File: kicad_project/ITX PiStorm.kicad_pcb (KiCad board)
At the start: 4 copper layers, 170 x 170 mm, 18 parts, among them J2 USB_67298-4090, J201 ATX-20, J3 DB9_Male_MountingHoles, J301 Conn_02x17_Odd_Even, J4 DB9_Male_MountingHoles, J5 HDMI_A_1.4, J6 DB15_Female_HighDensity, U301 74LVC06, U302 74LVC06, U303 74LVC14

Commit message: playground start
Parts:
- added U101: W25Q128JVS, Package_SO:SOIC-8_5.23x5.23mm_P1.27mm, F.Cu at (93.5, 158.8)
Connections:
- J201 pad 1: /Floppy Interface/+3.3V -> +3V3
- J201 pad 11: /Floppy Interface/+3.3V -> +3V3
- J201 pad 2: /Floppy Interface/+3.3V -> +3V3
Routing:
- net /Floppy Interface/+3.3V: track 42.5 -> 47.8 mm
- net /Floppy Interface/~{MTRON}: track 22.7 -> 21.9 mm

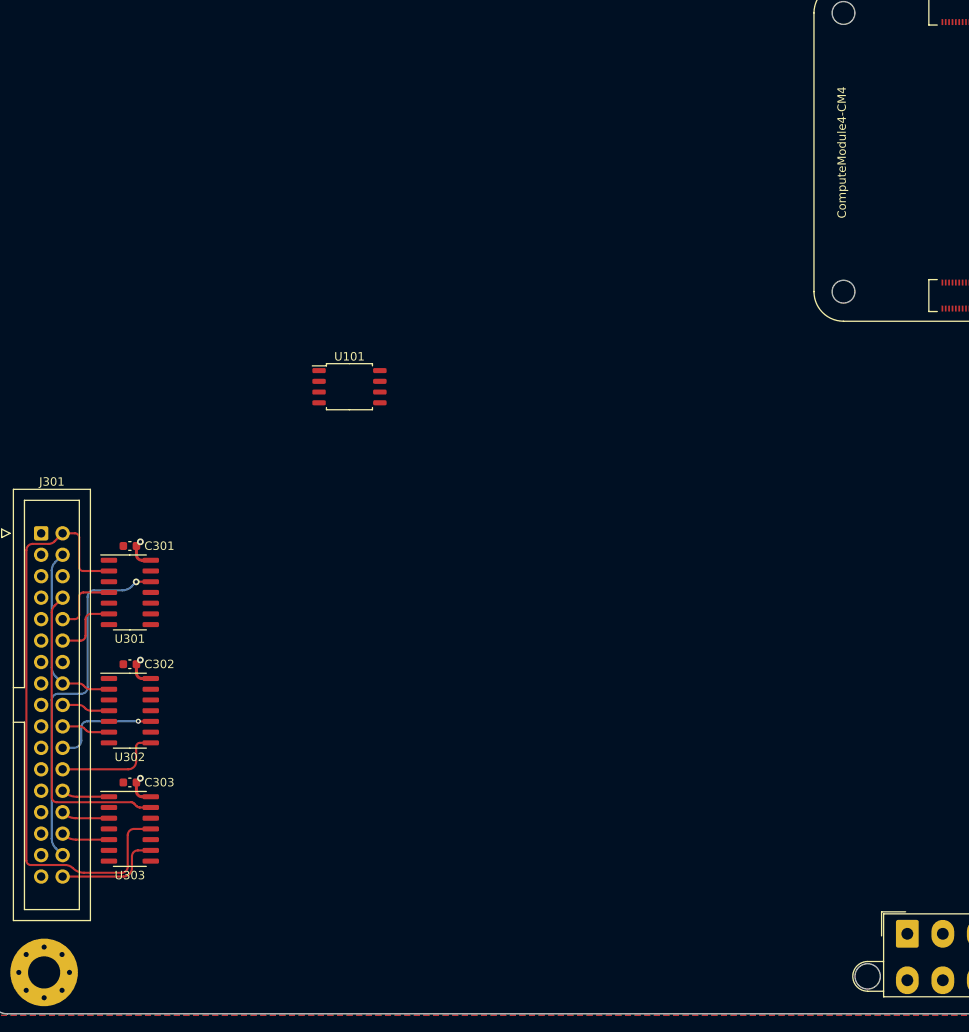
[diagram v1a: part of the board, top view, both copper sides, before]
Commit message: added ecp5 fpga without anything connected yet, added power to fpga
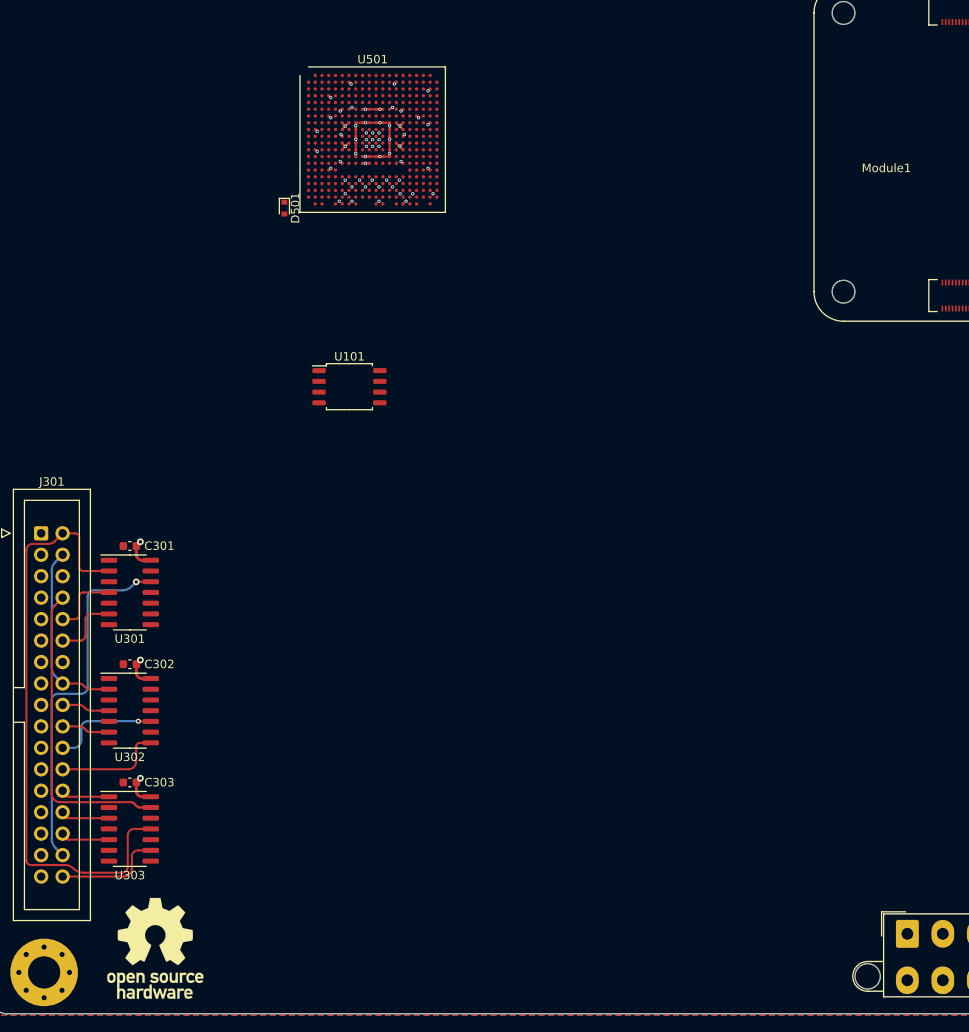
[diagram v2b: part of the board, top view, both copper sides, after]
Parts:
- added D501: 1N4148WT, Diode_SMD:D_SOD-523, F.Cu at (85.8, 137.6)
- added REF**: OSHW-Logo_11.4x12mm_SilkScreen, Symbol:OSHW-Logo_11.4x12mm_SilkScreen, F.Cu at (70.5, 225.2)
- added U501: LFE5U-85F-6BG381x, Package_BGA:Lattice_caBGA-381_17.0x17.0mm_Layout20x20_P0.8mm_Ball0.4mm_Pad0.4mm_NSMD, F.Cu at (96.2, 129.5)
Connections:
- C301 pad 1: /Floppy Interface/+3.3V -> +3V3
- C302 pad 1: /Floppy Interface/+3.3V -> +3V3
- C303 pad 1: /Floppy Interface/+3.3V -> +3V3
- U301 pad 14: /Floppy Interface/+3.3V -> +3V3
- U302 pad 14: /Floppy Interface/+3.3V -> +3V3
- U303 pad 14: /Floppy Interface/+3.3V -> +3V3
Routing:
- net +3V3: track 0.00 -> 57.9 mm, vias 0 -> 10
- net /Floppy Interface/+3.3V: track 47.8 -> 0.00 mm, vias 3 -> 0
- net +2V5: track 0.00 -> 26.9 mm, vias 0 -> 4
- net +1V2: track 0.00 -> 15.2 mm, vias 0 -> 10
- net GND: track 0.00 -> 3.54 mm, vias 0 -> 41
- added copper zone on In2.Cu, net +1V2
- added copper zone on In2.Cu, net +3V3
- removed copper zone on In2.Cu, net /Floppy Interface/+3.3V

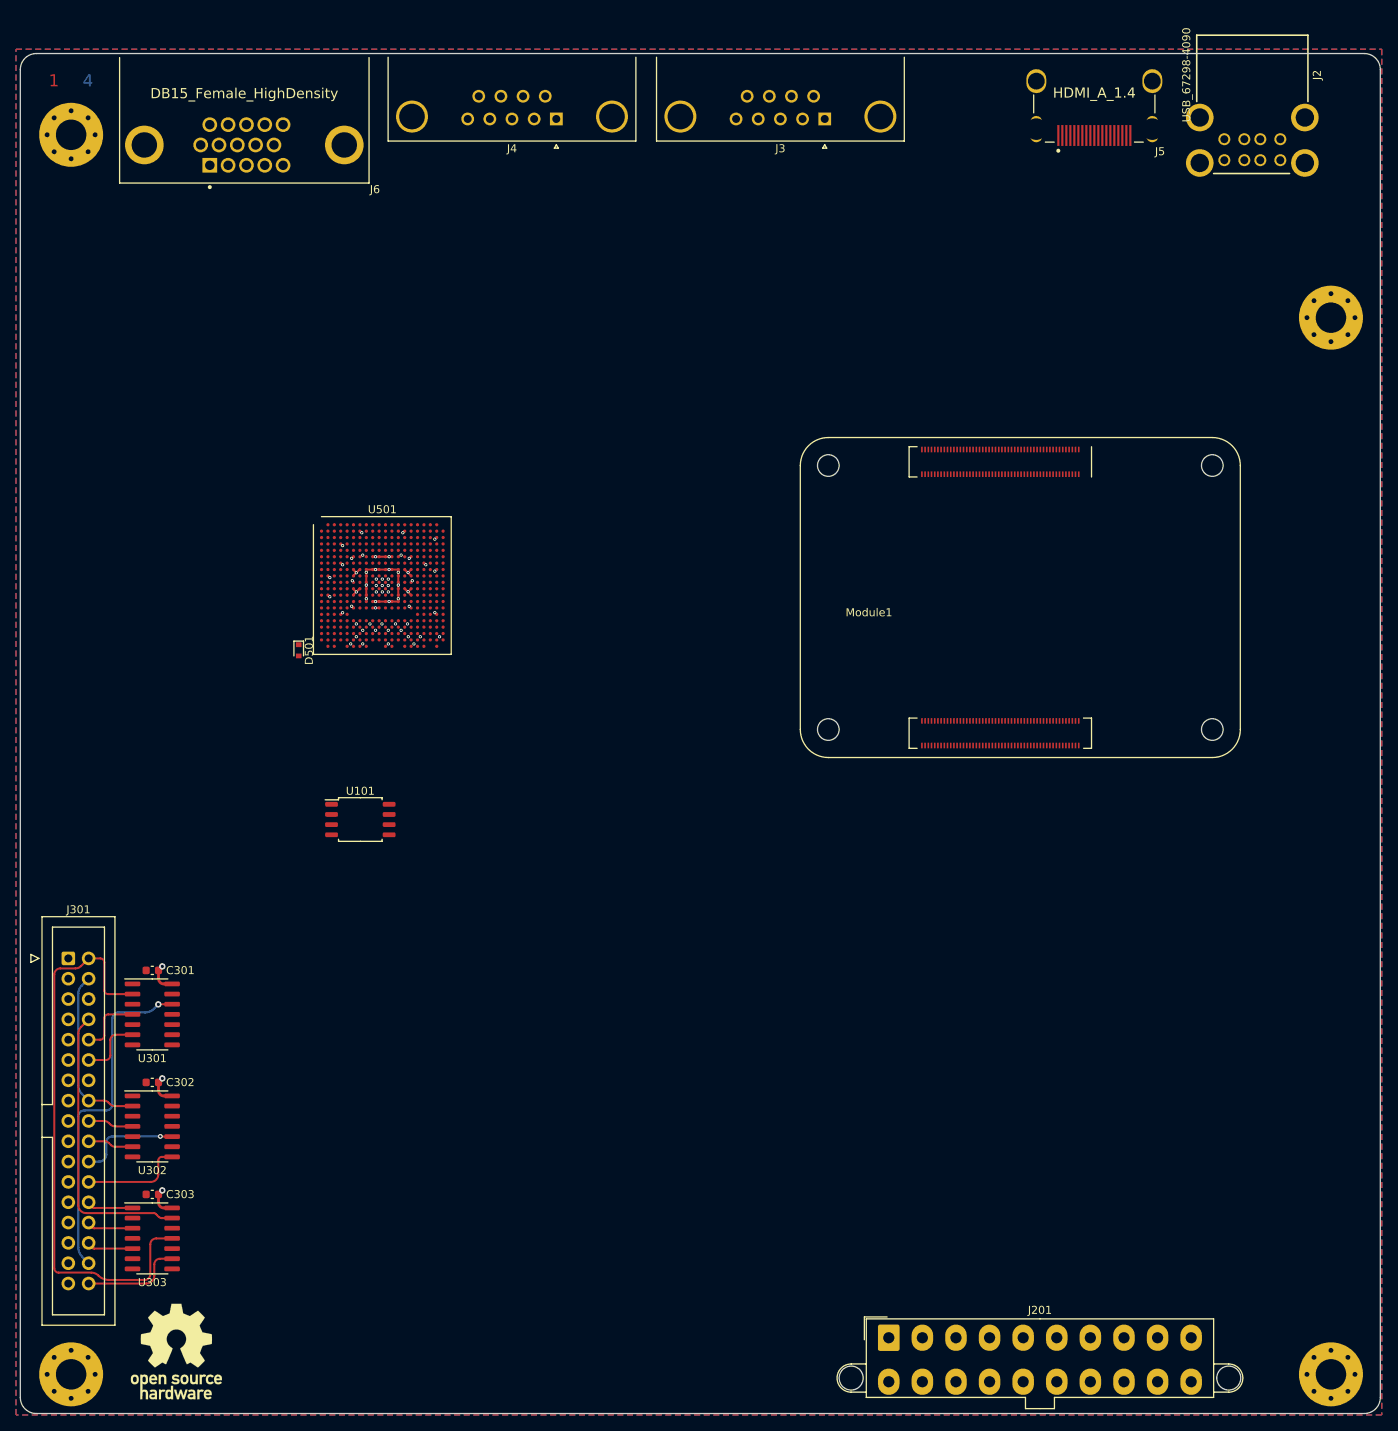
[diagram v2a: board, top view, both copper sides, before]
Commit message: added bits and pieces: a bit of memory, a bit of 1.1V power
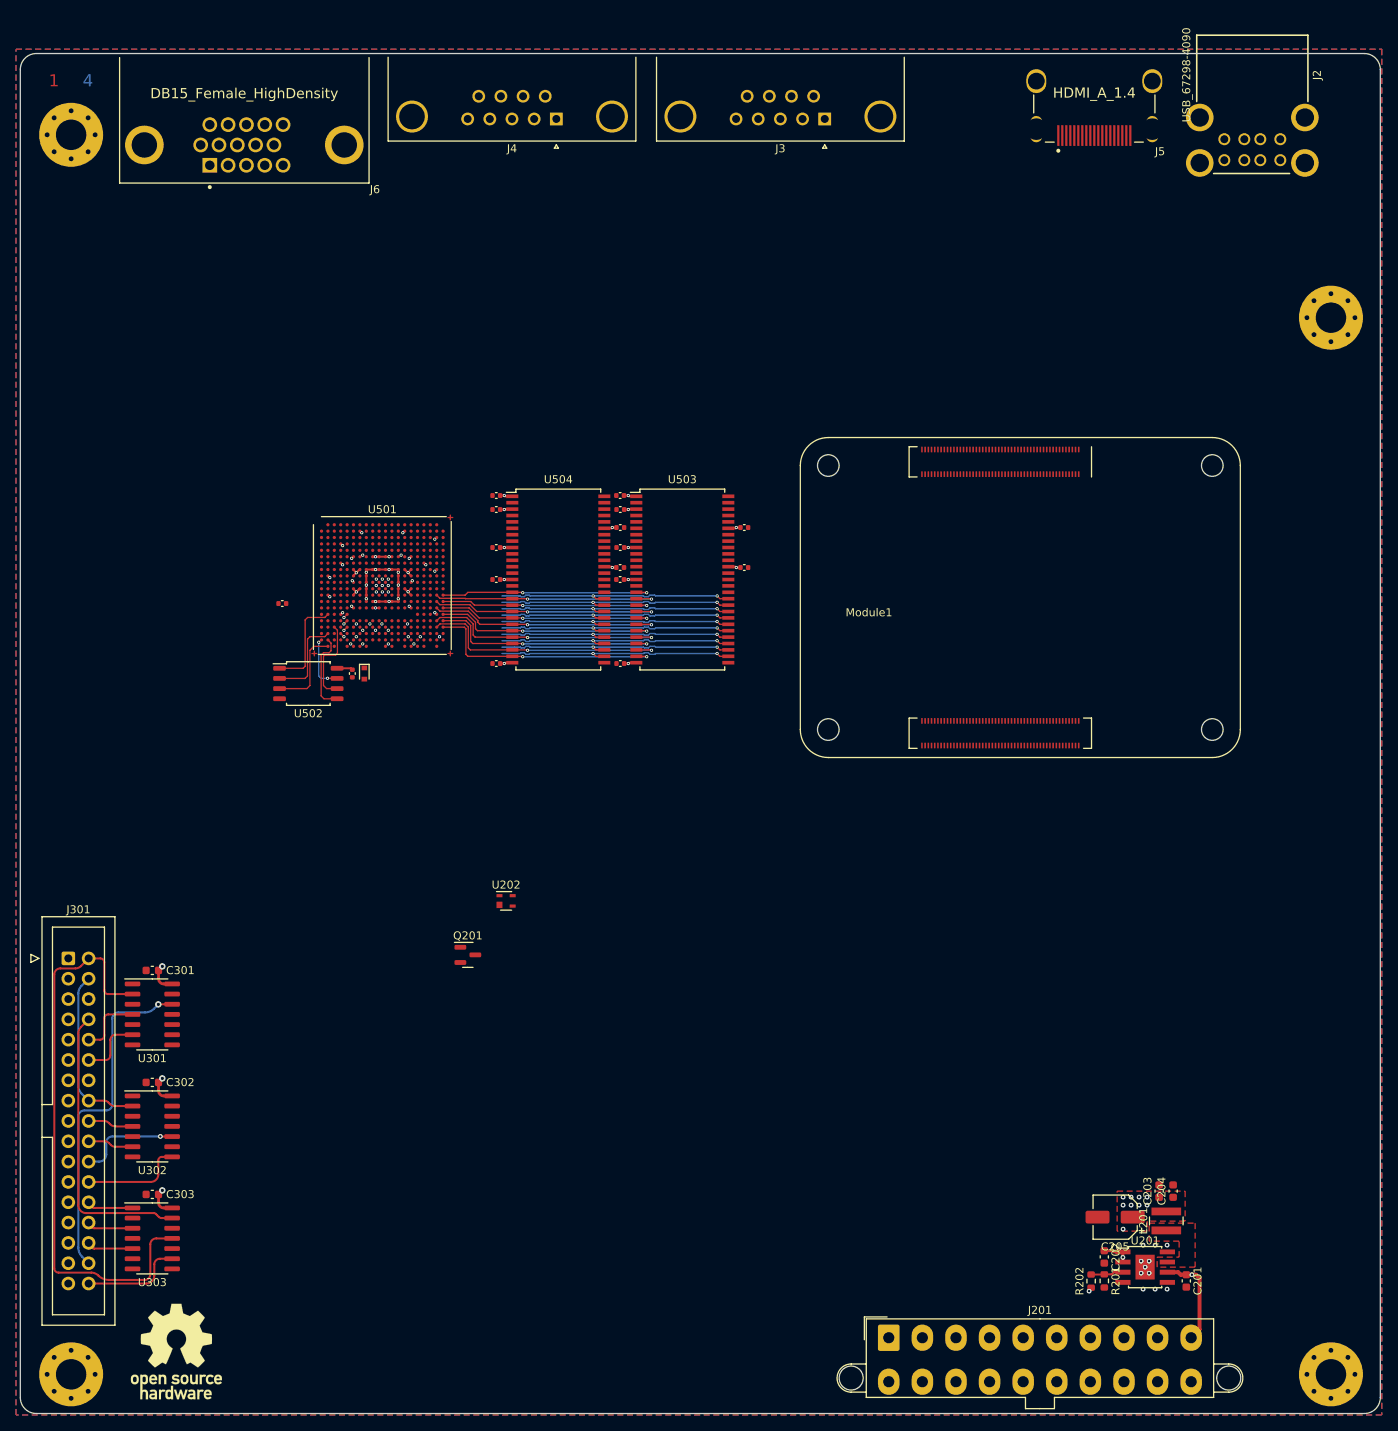
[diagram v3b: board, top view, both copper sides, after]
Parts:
- removed U101: W25Q128JVS, Package_SO:SOIC-8_5.23x5.23mm_P1.27mm
- added C201: 10µ, Capacitor_SMD:C_0603_1608Metric, F.Cu at (196.7, 216.4)
- added C202: 100nF, Capacitor_SMD:C_0603_1608Metric, F.Cu at (186.5, 213.4)
- added C203: 22µ, Capacitor_SMD:C_0603_1608Metric, F.Cu at (193.3, 205.2)
- added C204: 22µ, Capacitor_SMD:C_0603_1608Metric, F.Cu at (195.1, 205.2)
- added C205: 100µ, Capacitor_SMD:CP_Elec_5x5.9, F.Cu at (187.8, 208.4)
- added C501: 100nF, Capacitor_SMD:C_0402_1005Metric, F.Cu at (92.5, 140.5)
- added C502: 100nF, Capacitor_SMD:C_0402_1005Metric, F.Cu at (83.8, 131.8)
- added C503: 100nF, Capacitor_SMD:C_0402_1005Metric, F.Cu at (110.5, 128.8)
- added C504: 100nF, Capacitor_SMD:C_0402_1005Metric, F.Cu at (110.5, 124.8)
- added C505: 100nF, Capacitor_SMD:C_0402_1005Metric, F.Cu at (126.0, 127.2)
- added C506: 100nF, Capacitor_SMD:C_0402_1005Metric, F.Cu at (110.5, 120.0)
- added C507: 100nF, Capacitor_SMD:C_0402_1005Metric, F.Cu at (126.0, 122.2)
- added C508: 100nF, Capacitor_SMD:C_0402_1005Metric, F.Cu at (110.5, 118.2)
- added C509: 100nF, Capacitor_SMD:C_0402_1005Metric, F.Cu at (110.5, 139.2)
- added C510: 100nF, Capacitor_SMD:C_0402_1005Metric, F.Cu at (126.0, 124.8)
- added C511: 100nF, Capacitor_SMD:C_0402_1005Metric, F.Cu at (126.0, 120.0)
- added C512: 100nF, Capacitor_SMD:C_0402_1005Metric, F.Cu at (126.0, 128.8)
- added C513: 100nF, Capacitor_SMD:C_0402_1005Metric, F.Cu at (126.0, 118.2)
- added C514: 100nF, Capacitor_SMD:C_0402_1005Metric, F.Cu at (126.0, 139.2)
- added C515: 100nF, Capacitor_SMD:C_0402_1005Metric, F.Cu at (141.5, 127.2)
- added C516: 100nF, Capacitor_SMD:C_0402_1005Metric, F.Cu at (141.5, 122.2)
- added L201: 2.2µ, Inductor_SMD:L_Wuerth_MAPI-4030, F.Cu at (194.2, 208.9)
- added Q201: DMG2301L, Package_TO_SOT_SMD:SOT-23, F.Cu at (106.9, 175.7)
- added R201: 20k, Resistor_SMD:R_0603_1608Metric, F.Cu at (186.5, 216.4)
- added R202: 7k5, Resistor_SMD:R_0603_1608Metric, F.Cu at (184.8, 216.4)
- added U201: ST1S10PHR, Package_SO:TI_SO-PowerPAD-8, F.Cu at (191.6, 214.7)
- added U202: ADCMP350, Package_TO_SOT_SMD:Analog_KS-4, F.Cu at (111.7, 168.9)
- added U502: W25Q128JVS, Package_SO:SOIC-8_5.23x5.23mm_P1.27mm, F.Cu at (87.0, 141.8)
- added U503: MT48LC16M16A2P, Package_SO:TSOP-II-54_22.2x10.16mm_P0.8mm, F.Cu at (133.8, 128.8)
- added U504: MT48LC16M16A2P, Package_SO:TSOP-II-54_22.2x10.16mm_P0.8mm, F.Cu at (118.2, 128.8)
- moved D501 8.70 mm to (94.0, 140.5)
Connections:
- net +1V2 renamed +1V1
- U501 pad M19: unconnected-(U501-PadM19) -> /Memory and Bus Interface/~{CAS}
- U501 pad M20: unconnected-(U501-PadM20) -> /Memory and Bus Interface/~{WE}
- U501 pad N19: unconnected-(U501-PadN19) -> /Memory and Bus Interface/~{CS}
- U501 pad N20: unconnected-(U501-PadN20) -> /Memory and Bus Interface/~{RAS}
- U501 pad P19: unconnected-(U501-PadP19) -> /Memory and Bus Interface/BA1
- U501 pad P20: unconnected-(U501-PadP20) -> /Memory and Bus Interface/BA0
- U501 pad R2: unconnected-(U501-PadR2) -> Net-(U501-PadR2)
- U501 pad R20: unconnected-(U501-PadR20) -> /Memory and Bus Interface/A10
- U501 pad T19: unconnected-(U501-PadT19) -> /Memory and Bus Interface/A0
- U501 pad T20: unconnected-(U501-PadT20) -> /Memory and Bus Interface/A1
- U501 pad T4: unconnected-(U501-PadT4) -> +3V3
- U501 pad U19: unconnected-(U501-PadU19) -> /Memory and Bus Interface/A2
- U501 pad U20: unconnected-(U501-PadU20) -> /Memory and Bus Interface/A3
- U501 pad U3: unconnected-(U501-PadU3) -> Net-(U501-PadU3)
- U501 pad V2: unconnected-(U501-PadV2) -> Net-(U501-PadV2)
- U501 pad W1: unconnected-(U501-PadW1) -> Net-(U501-PadW1)
- U501 pad W2: unconnected-(U501-PadW2) -> Net-(U501-PadW2)
- U501 pad Y2: unconnected-(U501-PadY2) -> Net-(U501-PadY2)
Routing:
- net /Memory and Bus Interface/A2: track 0.00 -> 31.8 mm, vias 0 -> 2
- net /Memory and Bus Interface/A0: track 0.00 -> 30.8 mm, vias 0 -> 2
- net /Memory and Bus Interface/A11: track 0.00 -> 30.3 mm, vias 0 -> 2
- net /Memory and Bus Interface/A5: track 0.00 -> 30.3 mm, vias 0 -> 2
- net /Memory and Bus Interface/CLK: track 0.00 -> 30.3 mm, vias 0 -> 2
- net /Memory and Bus Interface/A8: track 0.00 -> 30.3 mm, vias 0 -> 2
- net /Memory and Bus Interface/A4: track 0.00 -> 30.3 mm, vias 0 -> 2
- net /Memory and Bus Interface/CKE: track 0.00 -> 30.3 mm, vias 0 -> 2
- net /Memory and Bus Interface/A9: track 0.00 -> 30.3 mm, vias 0 -> 2
- net /Memory and Bus Interface/A7: track 0.00 -> 30.3 mm, vias 0 -> 2
- net /Memory and Bus Interface/A6: track 0.00 -> 30.3 mm, vias 0 -> 2
- net /Memory and Bus Interface/A12: track 0.00 -> 30.3 mm, vias 0 -> 2
- net /Memory and Bus Interface/A3: track 0.00 -> 30.2 mm, vias 0 -> 2
- net /Memory and Bus Interface/BA1: track 0.00 -> 29.8 mm, vias 0 -> 2
- net /Memory and Bus Interface/~{CS}: track 0.00 -> 29.3 mm, vias 0 -> 2
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- added copper zone on F.Cu, net +1V1
- added copper zone on F.Cu, net Net-(L201-Pad1)

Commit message: minor wip updates
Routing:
- net /Memory and Bus Interface/BA1: track 29.8 -> 30.3 mm
- net +3V3: vias 24 -> 25
- removed copper zone on In2.Cu, net GND
